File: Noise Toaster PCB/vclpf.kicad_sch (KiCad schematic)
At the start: 20 parts, among them Q5 2N5457, U2 LM324, X12 Conn_01x01_Pin

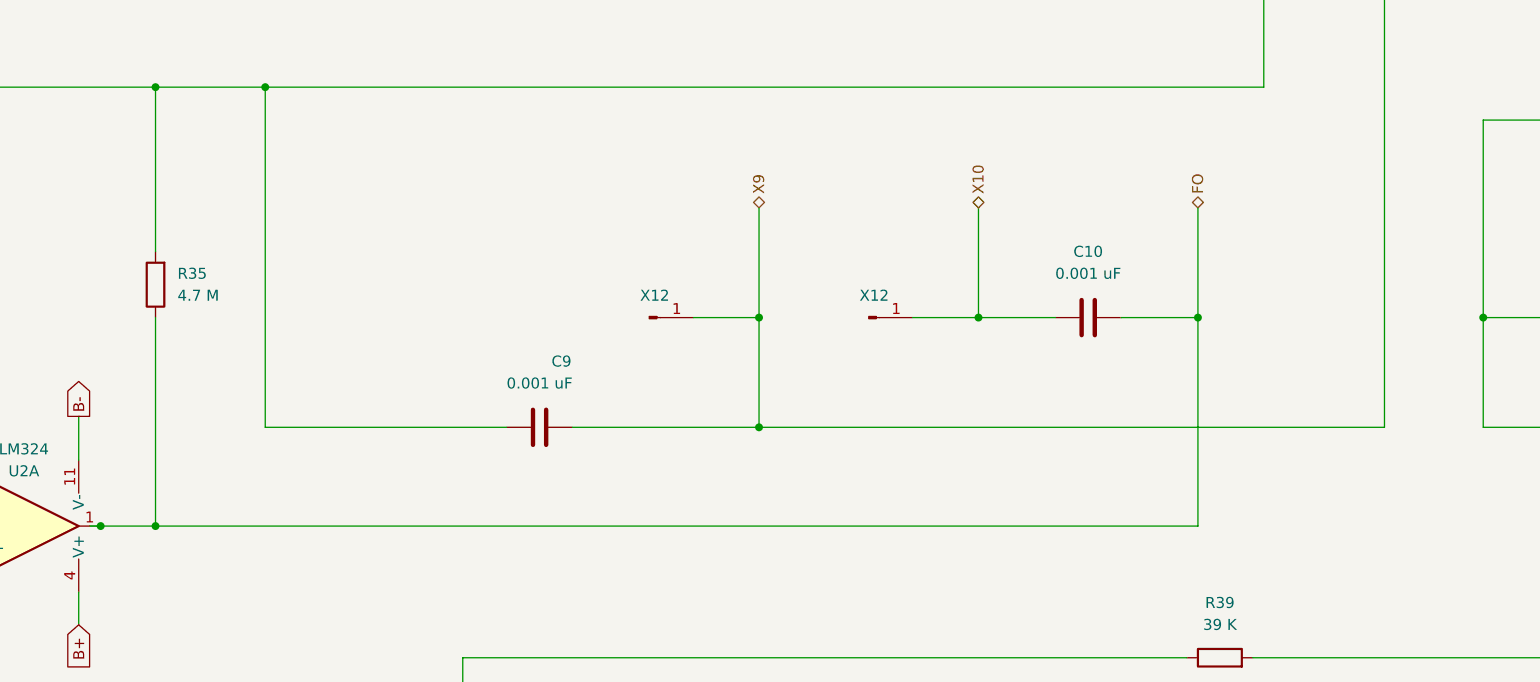
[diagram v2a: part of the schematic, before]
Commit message: refactored schematics and added front panel
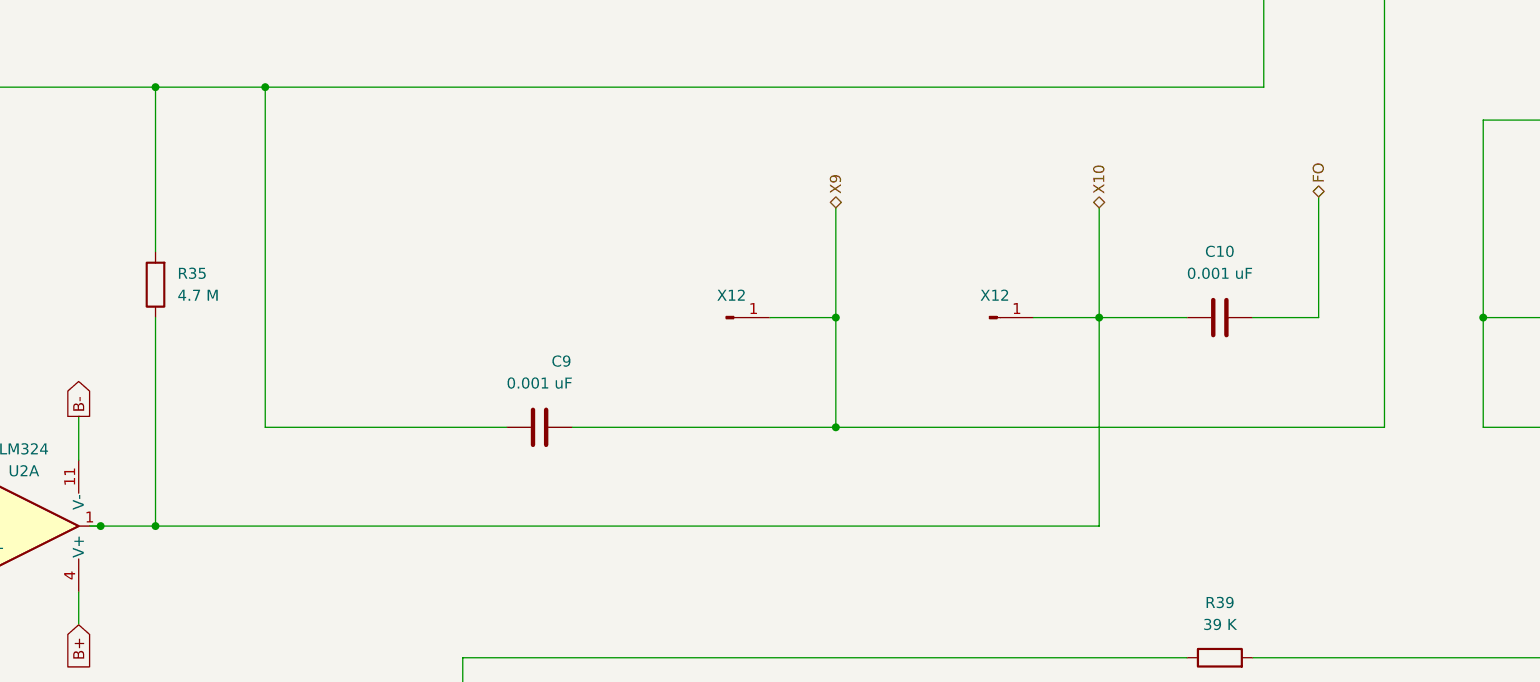
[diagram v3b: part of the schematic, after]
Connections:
- net FO: no longer R35.1, U2.1
- net X10: now also R35.1, U2.1
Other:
- moved on the sheet: X12
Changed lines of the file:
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@@
   (junction (at 139.7 38.1) (diameter 0) (color 0 0 0 0)
   )
+  (junction (at 135.89 127) (diameter 0) (color 0 0 0 0)
+  )
   (junction (at 50.8 138.43) (diameter 0) (color 0 0 0 0)
   )
-  (junction (at 127 114.3) (diameter 0) (color 0 0 0 0)
+  (junction (at 135.89 114.3) (diameter 0) (color 0 0 0 0)
   )
   (junction (at 43.18 38.1) (diameter 0) (color 0 0 0 0)
@@
   (junction (at 236.22 91.44) (diameter 0) (color 0 0 0 0)
   )
-  (junction (at 152.4 114.3) (diameter 0) (color 0 0 0 0)
-  )
-  (junction (at 127 127) (diameter 0) (color 0 0 0 0)
-  )
   (junction (at 95.25 52.07) (diameter 0) (color 0 0 0 0)
   )
@@
   (junction (at 92.71 170.18) (diameter 0) (color 0 0 0 0)
   )
-  (junction (at 177.8 114.3) (diameter 0) (color 0 0 0 0)
+  (junction (at 166.37 114.3) (diameter 0) (color 0 0 0 0)
   )
   (junction (at 69.85 87.63) (diameter 0) (color 0 0 0 0)
@@
     (stroke (width 0) (type default))
   )
-  (wire (pts (xy 177.8 101.6) (xy 177.8 114.3))
-    (stroke (width 0) (type default))
-  )
   (wire (pts (xy 31.75 140.97) (xy 31.75 149.86))
     (stroke (width 0) (type default))
@@
     (stroke (width 0) (type default))
   )
-  (wire (pts (xy 177.8 114.3) (xy 177.8 138.43))
+  (wire (pts (xy 166.37 114.3) (xy 166.37 138.43))
     (stroke (width 0) (type default))
   )
@@
     (stroke (width 0) (type default))
   )
-  (wire (pts (xy 152.4 114.3) (xy 161.29 114.3))
-    (stroke (width 0) (type default))
-  )
   (wire (pts (xy 63.5 54.61) (xy 63.5 52.07))
     (stroke (width 0) (type default))
@@
     (stroke (width 0) (type default))
   )
-  (wire (pts (xy 127 114.3) (xy 127 127))
+  (wire (pts (xy 135.89 114.3) (xy 135.89 127))
     (stroke (width 0) (type default))
   )
@@
     (stroke (width 0) (type default))
   )
+  (wire (pts (xy 166.37 114.3) (xy 176.53 114.3))
+    (stroke (width 0) (type default))
+  )
   (wire (pts (xy 92.71 153.67) (xy 92.71 170.18))
     (stroke (width 0) (type default))
@@
     (stroke (width 0) (type default))
   )
-  (wire (pts (xy 177.8 114.3) (xy 168.91 114.3))
-    (stroke (width 0) (type default))
-  )
   (wire (pts (xy 226.06 91.44) (xy 236.22 91.44))
     (stroke (width 0) (type default))
@@
     (stroke (width 0) (type default))
   )
-  (wire (pts (xy 57.15 138.43) (xy 177.8 138.43))
+  (wire (pts (xy 57.15 138.43) (xy 166.37 138.43))
     (stroke (width 0) (type default))
   )
@@
     (stroke (width 0) (type default))
   )
-  (wire (pts (xy 199.39 127) (xy 127 127))
+  (wire (pts (xy 199.39 127) (xy 135.89 127))
     (stroke (width 0) (type default))
   )
@@
     (stroke (width 0) (type default))
   )
-  (wire (pts (xy 119.38 114.3) (xy 127 114.3))
-    (stroke (width 0) (type default))
-  )
-  (wire (pts (xy 152.4 101.6) (xy 152.4 114.3))
+  (wire (pts (xy 128.27 114.3) (xy 135.89 114.3))
+    (stroke (width 0) (type default))
+  )
+  (wire (pts (xy 166.37 101.6) (xy 166.37 114.3))
     (stroke (width 0) (type default))
   )
@@
     (stroke (width 0) (type default))
   )
-  (wire (pts (xy 144.78 114.3) (xy 152.4 114.3))
+  (wire (pts (xy 158.75 114.3) (xy 166.37 114.3))
     (stroke (width 0) (type default))
   )
@@
     (stroke (width 0) (type default))
   )
+  (wire (pts (xy 191.77 114.3) (xy 184.15 114.3))
+    (stroke (width 0) (type default))
+  )
   (wire (pts (xy 69.85 127) (xy 69.85 87.63))
     (stroke (width 0) (type default))
@@
     (stroke (width 0) (type default))
   )
-  (wire (pts (xy 127 101.6) (xy 127 114.3))
+  (wire (pts (xy 135.89 101.6) (xy 135.89 114.3))
     (stroke (width 0) (type default))
   )
@@
     (stroke (width 0) (type default))
   )
-  (wire (pts (xy 105.41 127) (xy 127 127))
+  (wire (pts (xy 105.41 127) (xy 135.89 127))
     (stroke (width 0) (type default))
   )
   (wire (pts (xy 35.56 72.39) (xy 95.25 72.39))
+    (stroke (width 0) (type default))
+  )
+  (wire (pts (xy 191.77 100.33) (xy 191.77 114.3))
     (stroke (width 0) (type default))
   )
@@
     )
   )
-  (hierarchical_label "FO" (shape bidirectional) (at 177.8 101.6 90) (fields_autoplaced)
+  (hierarchical_label "FO" (shape bidirectional) (at 191.77 100.33 90) (fields_autoplaced)
     (effects (font (size 1.27 1.27)) (justify left))
   )
@@
     (effects (font (size 1.27 1.27)) (justify right))
   )
-  (hierarchical_label "X9" (shape bidirectional) (at 127 101.6 90) (fields_autoplaced)
+  (hierarchical_label "X9" (shape bidirectional) (at 135.89 101.6 90) (fields_autoplaced)
     (effects (font (size 1.27 1.27)) (justify left))
   )
@@
     (effects (font (size 1.27 1.27)) (justify right))
   )
-  (hierarchical_label "X10" (shape bidirectional) (at 152.4 101.6 90) (fields_autoplaced)
+  (hierarchical_label "X10" (shape bidirectional) (at 166.37 101.6 90) (fields_autoplaced)
     (effects (font (size 1.27 1.27)) (justify left))
   )
@@
     )
   )
+  (symbol (lib_id "Device:C") (at 180.34 114.3 90) (unit 1)
+    (in_bom yes) (on_board yes) (dnp no) (fields_autoplaced)
+    (property "Reference" "C10" (at 180.34 106.68 90)
+      (effects (font (size 1.27 1.27)))
+    )
+    (property "Value" "0.001 uF" (at 180.34 109.22 90)
+      (effects (font (size 1.27 1.27)))
+    )
+    (property "Footprint" "" (at 184.15 113.3348 0)
+      (effects (font (size 1.27 1.27)) hide)
+    )
+    (property "Datasheet" "~" (at 180.34 114.3 0)
+      (effects (font (size 1.27 1.27)) hide)
+    )
+    (pin "1")
+    (pin "2")
+    (instances
+      (project "Noise Toaster PCB"
+        (path "/7be3f398-d902-4566-9ee4-0bff072cd47e/3fdee3e7-d1eb-4d7e-b78f-578001cef6ab"
+          (reference "C10") (unit 1)
+        )
+        (path "/7be3f398-d902-4566-9ee4-0bff072cd47e/3dc41d81-2fd5-4e3e-87af-deba83358964"
+          (reference "C10") (unit 1)
+        )
+      )
+    )
+  )
   (symbol (lib_id "Connector:Conn_01x01_Pin") (at 114.3 52.07 180) (unit 1)
     (in_bom yes) (on_board yes) (dnp no)
@@
     )
   )
-  (symbol (lib_id "Connector:Conn_01x01_Pin") (at 139.7 114.3 0) (unit 1)
-    (in_bom yes) (on_board yes) (dnp no) (fields_autoplaced)
-    (property "Reference" "X12" (at 140.335 111.76 0)
-      (effects (font (size 1.27 1.27)))
-    )
-    (property "Value" "Conn_01x01_Pin" (at 141.605 113.03 90)
-      (effects (font (size 1.27 1.27)) (justify left) hide)
-    )
-    (property "Footprint" "" (at 139.7 114.3 0)
-      (effects (font (size 1.27 1.27)) hide)
-    )
-    (property "Datasheet" "~" (at 139.7 114.3 0)
+  (symbol (lib_id "Connector:Conn_01x01_Pin") (at 153.67 114.3 0) (unit 1)
+    (in_bom yes) (on_board yes) (dnp no) (fields_autoplaced)
+    (property "Reference" "X12" (at 154.305 111.76 0)
+      (effects (font (size 1.27 1.27)))
+    )
+    (property "Value" "Conn_01x01_Pin" (at 155.575 113.03 90)
+      (effects (font (size 1.27 1.27)) (justify left) hide)
+    )
+    (property "Footprint" "" (at 153.67 114.3 0)
+      (effects (font (size 1.27 1.27)) hide)
+    )
+    (property "Datasheet" "~" (at 153.67 114.3 0)
       (effects (font (size 1.27 1.27)) hide)
     )
@@
     )
   )
-  (symbol (lib_id "Connector:Conn_01x01_Pin") (at 114.3 114.3 0) (unit 1)
-    (in_bom yes) (on_board yes) (dnp no) (fields_autoplaced)
-    (property "Reference" "X12" (at 114.935 111.76 0)
-      (effects (font (size 1.27 1.27)))
-    )
-    (property "Value" "Conn_01x01_Pin" (at 116.205 113.03 90)
-      (effects (font (size 1.27 1.27)) (justify left) hide)
-    )
-    (property "Footprint" "" (at 114.3 114.3 0)
-      (effects (font (size 1.27 1.27)) hide)
-    )
-    (property "Datasheet" "~" (at 114.3 114.3 0)
+  (symbol (lib_id "Connector:Conn_01x01_Pin") (at 123.19 114.3 0) (unit 1)
+    (in_bom yes) (on_board yes) (dnp no) (fields_autoplaced)
+    (property "Reference" "X12" (at 123.825 111.76 0)
+      (effects (font (size 1.27 1.27)))
+    )
+    (property "Value" "Conn_01x01_Pin" (at 125.095 113.03 90)
+      (effects (font (size 1.27 1.27)) (justify left) hide)
+    )
+    (property "Footprint" "" (at 123.19 114.3 0)
+      (effects (font (size 1.27 1.27)) hide)
+    )
+    (property "Datasheet" "~" (at 123.19 114.3 0)
       (effects (font (size 1.27 1.27)) hide)
     )
@@
         )
       )
-    )
-  )
-  (symbol (lib_id "Device:C") (at 165.1 114.3 90) (unit 1)
-    (in_bom yes) (on_board yes) (dnp no) (fields_autoplaced)
-    (property "Reference" "C10" (at 165.1 106.68 90)
-      (effects (font (size 1.27 1.27)))
-    )
-    (property "Value" "0.001 uF" (at 165.1 109.22 90)
-      (effects (font (size 1.27 1.27)))
-    )
-    (property "Footprint" "" (at 168.91 113.3348 0)
-      (effects (font (size 1.27 1.27)) hide)
-    )
-    (property "Datasheet" "~" (at 165.1 114.3 0)
-      (effects (font (size 1.27 1.27)) hide)
-    )
-    (pin "1")
-    (pin "2")
-    (instances
-      (project "Noise Toaster PCB"
-        (path "/7be3f398-d902-4566-9ee4-0bff072cd47e/3fdee3e7-d1eb-4d7e-b78f-578001cef6ab"
-          (reference "C10") (unit 1)
-        )
-      )

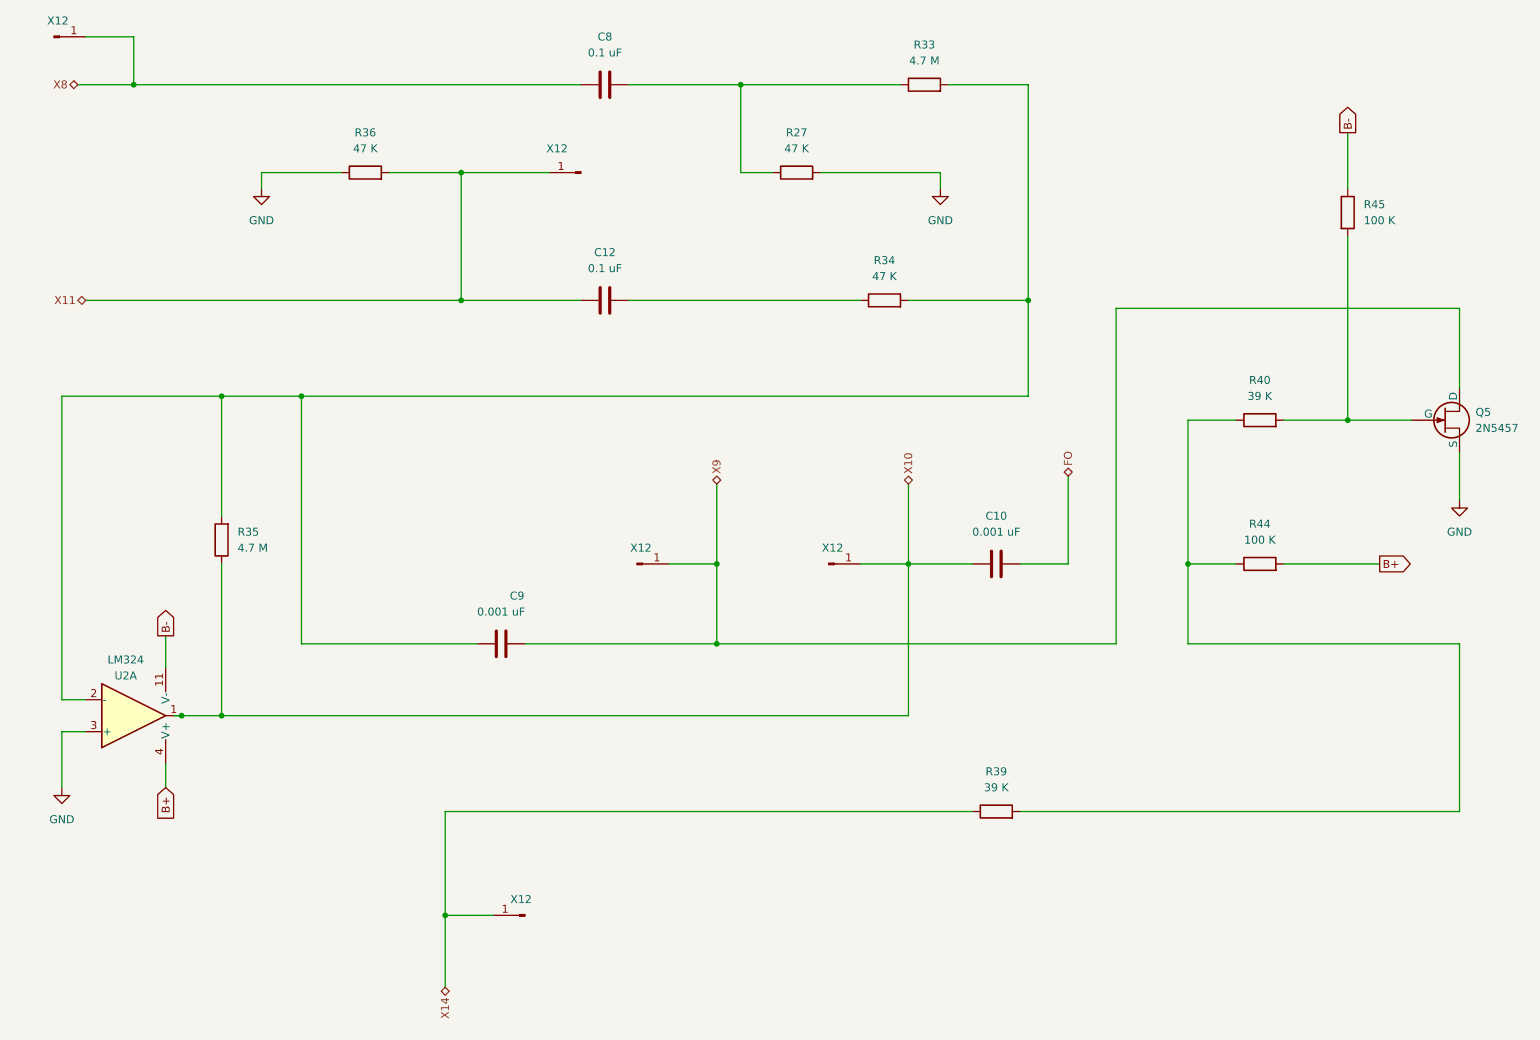
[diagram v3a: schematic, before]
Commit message: wireing and components have been checked
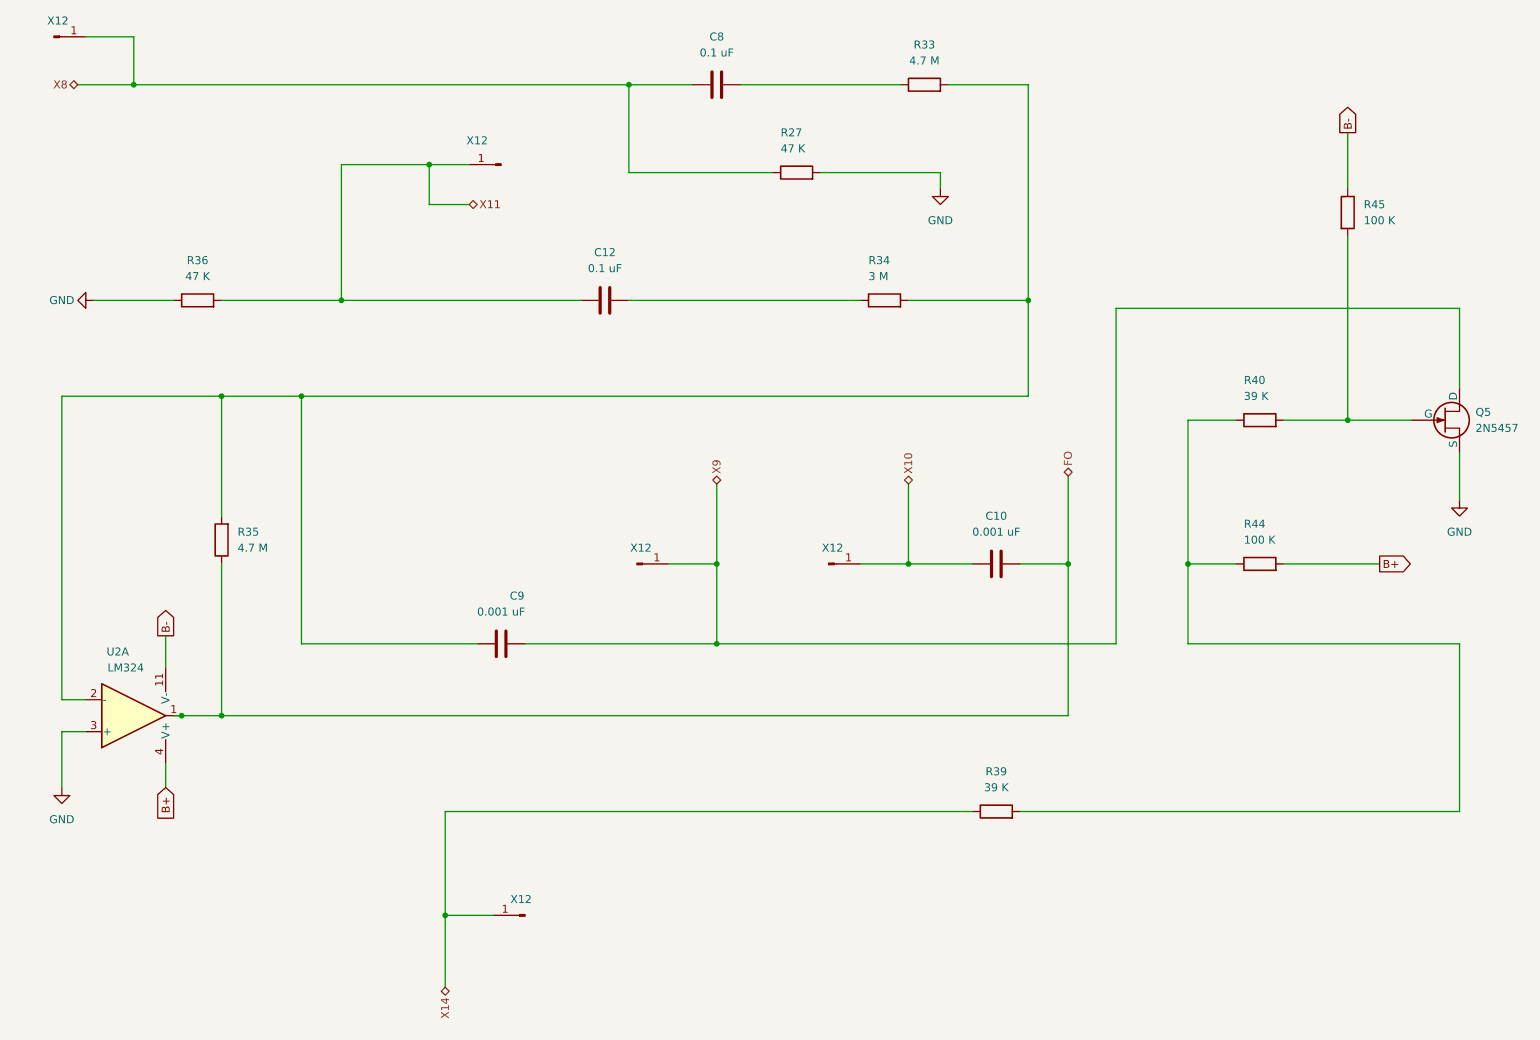
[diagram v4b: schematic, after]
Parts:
- R34: value 47 K -> 3 M
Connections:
- net FO: now also R35.1, U2.1
- net X10: no longer R35.1, U2.1
- net X8: now also R27.1
- net at C8.2, R33.1: no longer R27.1
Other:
- moved on the sheet: C8, R36, X12
